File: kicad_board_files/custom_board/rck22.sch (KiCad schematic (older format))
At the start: 75 parts, among them IC1 PEC11L-4115F-S0020, J1 Conn_02x05_Odd_Even, J10 Conn_01x02, J2 USB_OTG, J3 PCC-SMP-K, J4 5V_DC_IN, J5 header, J6 SSR, J7 SSR, J8 SSR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

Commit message: Tweak the PCB silkscreen, add main UI graphic
Add some silkscreen text with version number and Logos
Add a graphic to be loaded from SD card for the main UI before reflow graph
Tweak the PCB layout and export new images from the 3D viewer
Update the README
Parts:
- added R18: 680/±1%/0.1W/0402, Resistor_SMD:R_0402_1005Metric, symbol Device:R_Small
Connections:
- net +3V3: now also R18.1
- net SWD_IO: now also R18.2
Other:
- note removed: "Commit message: "Add protection to thermocouple input\n\nUpdate the thermocouple interface with ferrite beads and filter capacitor\nAdd an alternative thermocouple connector other than terminal block\nAdd extra SSR lines for the case of multiple heaters\nReplace the 700mA 3.3V regulator with a 1A regulator, and replace its capacitors\nAdd 10K series resistors to the rotary encoder ouputs\nReplace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"
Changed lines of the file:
@@
-$EndComp
-$Comp
-L Connector_Generic:Conn_02x05_Odd_Even J1
-U 1 1 5D372FAD
-P 4650 3900
-F 0 "J1" H 4700 4317 50  0000 C CNN
-F 1 "Conn_02x05_Odd_Even" H 4700 4226 50  0000 C CNN
-F 2 "Connector_PinHeader_1.27mm:PinHeader_2x05_P1.27mm_Vertical_SMD" H 4650 3900 50  0001 C CNN
-F 3 "https://datasheet.lcsc.com/szlcsc/1907251430_Amphenol-ICC-20021221-00010C4LF_C180221.pdf" H 4650 3900 50  0001 C CNN
-F 4 "20021221-00010C4LF" H 4650 3900 50  0001 C CNN "Mfr. #"
-F 5 "C180221" H 4650 3900 50  0001 C CNN "LCSC #"
-F 6 "140" H 4650 3900 50  0001 C CNN "Stock"
-	1    4650 3900
-	1    0    0    -1
 $EndComp
 $Comp
@@
 $EndComp
 $Comp
-L sdcard_1051620101:sdcard_1051620101 conn1
-U 1 1 5D393514
-P 5050 1050
-F 0 "conn1" H 5050 1450 60  0000 C CNN
-F 1 "sdcard_1051620101" H 5200 500 60  0000 C CNN
-F 2 "connectors:sdcard_1051620101" H 5050 1050 60  0001 C CNN
-F 3 "https://www.molex.com/pdm_docs/sd/1051620101_sd.pdf" H 5050 1050 60  0001 C CNN
-F 4 "1051620101 " H 5050 1050 50  0001 C CNN "Mfr. #"
-F 5 "WM12823CT-ND" H 5050 1050 50  0001 C CNN "DK #"
-	1    5050 1050
-	1    0    0    -1
-$EndComp
-$Comp
 L Connector:TestPoint_Alt TP1
 U 1 1 5D394552
@@
 Wire Wire Line
 	8550 1200 8600 1200
-Text GLabel 4600 900  0    50   Input ~ 0
-SD_CS
-Text GLabel 4600 1000 0    50   Input ~ 0
-SD_MOSI
-Text GLabel 4600 1100 0    50   Input ~ 0
-SD_CLK
-Text GLabel 4600 1200 0    50   Input ~ 0
-SD_MISO
-NoConn ~ 4600 800
-NoConn ~ 4600 1300
-$Comp
-L power:+3V3 #PWR0103
-U 1 1 5D3982BB
-P 6200 1150
-F 0 "#PWR0103" H 6200 1000 50  0001 C CNN
-F 1 "+3V3" H 6200 1300 50  0000 C CNN
-F 2 "" H 6200 1150 50  0001 C CNN
-F 3 "" H 6200 1150 50  0001 C CNN
-	1    6200 1150
-	1    0    0    -1
-$EndComp
-$Comp
-L Device:C_Small C7
-U 1 1 5D398822
-P 6200 1400
-F 0 "C7" H 6090 1465 50  0000 L CNN
-F 1 "22uF/6.3V/±20%/0603" H 5730 1340 25  0000 L CNN
-F 2 "Capacitor_SMD:C_0603_1608Metric" H 6200 1400 50  0001 C CNN
-F 3 "https://datasheet.lcsc.com/szlcsc/Murata-Electronics-GRM188R71E104KA01D_C77050.pdf" H 6200 1400 50  0001 C CNN
-F 4 "GRM188R71E104KA01D" H 6200 1400 50  0001 C CNN "Mfr. #"
-F 5 "C77050" H 6200 1400 50  0001 C CNN "LCSC #"
-F 6 "334500" H 6200 1400 50  0001 C CNN "Stock"
-	1    6200 1400
-	1    0    0    -1
-$EndComp
-$Comp
-L power:GND #PWR0104
-U 1 1 5D398E24
-P 6200 1550
-F 0 "#PWR0104" H 6200 1300 50  0001 C CNN
-F 1 "GND" H 6205 1377 50  0000 C CNN
-F 2 "" H 6200 1550 50  0001 C CNN
-F 3 "" H 6200 1550 50  0001 C CNN
-	1    6200 1550
-	1    0    0    -1
-$EndComp
-$Comp
-L power:GND #PWR0105
-U 1 1 5D39A30B
-P 6100 850
-F 0 "#PWR0105" H 6100 600 50  0001 C CNN
-F 1 "GND" H 6105 677 50  0000 C CNN
-F 2 "" H 6100 850 50  0001 C CNN
-F 3 "" H 6100 850 50  0001 C CNN
-	1    6100 850
-	0    -1   -1   0
-$EndComp
-Wire Wire Line
-	5750 850  5950 850
-Wire Wire Line
-	5750 950  5950 950
-Wire Wire Line
-	6200 1150 6200 1200
-Wire Wire Line
-	5750 1200 6200 1200
-Connection ~ 6200 1200
-Text GLabel 5750 1100 2    50   Input ~ 0
-SD_SW
 $Comp
 L Device:C_Small C5
@@
 	0    -1   -1   0
 $EndComp
-Text GLabel 4950 3700 2    50   Input ~ 0
-SWD_IO
 Text GLabel 4950 3800 2    50   Input ~ 0
 SWD_CLK
@@
 $EndComp
 Wire Wire Line
-	4200 3700 4450 3700
+	4200 3700 4350 3700
 Text GLabel 4950 4000 2    50   Input ~ 0
 UART_RX
@@
 Connection ~ 1200 1550
 Wire Wire Line
-	5950 850  5950 950
-Wire Wire Line
-	6100 850  5950 850
-Connection ~ 5950 850
-Wire Wire Line
 	3600 7350 3600 7450
-Wire Wire Line
-	6200 1200 6200 1300
-Wire Wire Line
-	6200 1500 6200 1550
 Text GLabel 8200 4750 0    50   Input ~ 0
 SW
@@
 	1000 5950 1200 5950
 Connection ~ 1000 5950
-Text Notes 4100 1650 0    63   ~ 13
-SD Card
 Wire Notes Line
 	2991 6308 6805 6306
@@
 	4700 5550 4900 5550
 Connection ~ 4700 5550
-Text Notes 12450 2500 0    100  ~ 0
-Commit message: "Add protection to thermocouple input\n\nUpdate the thermocouple interface with ferrite beads and filter capacitor\nAdd an alternative thermocouple connector other than terminal block\nAdd extra SSR lines for the case of multiple heaters\nReplace the 700mA 3.3V regulator with a 1A regulator, and replace its capacitors\nAdd 10K series resistors to the rotary encoder ouputs\nReplace buttons with two pin header connectors so as to use momentary switches on the casing\nReverse UART connection in ARM SWD debug connector\nTune LED resistors to the datasheet parameters\nRearrange the schamtic and layout\nSource all components and generate a HTML BOM\nUpdate the README" \n
 $Comp
 L Power_Protection:NUP2105L D2
@@
 	8550 1050 8800 1050
 $Comp
-L myRF:karibe_logo L1
-U 1 1 5DD9A175
-P 1850 7150
-F 0 "L1" H 1737 7375 50  0000 C CNN
-F 1 "karibe_logo" H 1737 7284 50  0000 C CNN
-F 2 "artwork:karibe_logo" H 1850 7150 50  0001 C CNN
-F 3 "" H 1850 7150 50  0001 C CNN
-F 4 "1" H 1850 7150 50  0001 C CNN "DNP"
-	1    1850 7150
-	1    0    0    -1
-$EndComp
-$Comp
 L Graphic:Logo_Open_Hardware_Small #LOGO1
 U 1 1 5DDA873C
@@
 F 3 "~" H 10700 6850 50  0001 C CNN
 	1    10700 6850
-	1    0    0    -1
-$EndComp
-$Comp
-L power:GND #PWR0144
-U 1 1 5DDAE8C7
-P 1950 7150
-F 0 "#PWR0144" H 1950 6900 50  0001 C CNN
-F 1 "GND" H 1955 6977 50  0000 C CNN
-F 2 "" H 1950 7150 50  0001 C CNN
-F 3 "" H 1950 7150 50  0001 C CNN
-	1    1950 7150
 	1    0    0    -1
 $EndComp
@@
 Text Label 7850 3800 0    50   ~ 0
 DN
+Text GLabel 5050 3700 2    50   Input ~ 0
+SWD_IO
+$Comp
+L Connector_Generic:Conn_02x05_Odd_Even J1
+U 1 1 5D372FAD
+P 4650 3900
+F 0 "J1" H 4700 4200 50  0000 C CNN
+F 1 "Conn_02x05_Odd_Even" H 4850 3600 50  0000 C CNN
+F 2 "Connector_PinHeader_1.27mm:PinHeader_2x05_P1.27mm_Vertical_SMD" H 4650 3900 50  0001 C CNN
+F 3 "https://datasheet.lcsc.com/szlcsc/1907251430_Amphenol-ICC-20021221-00010C4LF_C180221.pdf" H 4650 3900 50  0001 C CNN
+F 4 "20021221-00010C4LF" H 4650 3900 50  0001 C CNN "Mfr. #"
+F 5 "C180221" H 4650 3900 50  0001 C CNN "LCSC #"
+F 6 "140" H 4650 3900 50  0001 C CNN "Stock"
+	1    4650 3900
+	1    0    0    -1
+$EndComp
+$Comp
+L Device:R_Small R18
+U 1 1 5DC1628C
+P 4700 3500
+F 0 "R18" V 4800 3450 50  0000 L CNN
+F 1 "680/±1%/0.1W/0402" V 4750 3300 25  0000 L CNN
+F 2 "Resistor_SMD:R_0402_1005Metric" H 4700 3500 50  0001 C CNN
+F 3 "https://datasheet.lcsc.com/szlcsc/1810191533_KOA-Speer-Elec-RK73H1ETTP6800F_C159998.pdf" H 4700 3500 50  0001 C CNN
+F 4 "RK73H1ETTP6800F" H 4700 3500 50  0001 C CNN "Mfr. #"
+F 5 "C159998" H 4700 3500 50  0001 C CNN "LCSC #"
+	1    4700 3500
+	0    -1   -1   0
+$EndComp
+Wire Wire Line
+	4950 3700 5000 3700
+Wire Wire Line
+	5000 3700 5000 3500
+Wire Wire Line
+	5000 3500 4800 3500
+Connection ~ 5000 3700
+Wire Wire Line
+	5000 3700 5050 3700
+Wire Wire Line
+	4600 3500 4350 3500
+Wire Wire Line
+	4350 3500 4350 3700
+Connection ~ 4350 3700
+Wire Wire Line
+	4350 3700 4450 3700
+$Comp
+L myRF:karibe_logo L1
+U 1 1 5DC493DB
+P 7350 6800
+F 0 "L1" H 7300 6700 50  0001 C CNN
+F 1 "karibe_logo" H 7350 6900 50  0001 C CNN
+F 2 "artwork:karibe_logo" H 7350 6800 50  0001 C CNN
+F 3 "" H 7350 6800 50  0001 C CNN
+F 4 "1" H 7350 6800 50  0001 C CNN "DNP"
+	1    7350 6800
+	1    0    0    -1
+$EndComp
+Text Notes 3905 1695 0    63   ~ 13
+SD Card
+Wire Wire Line
+	6200 1500 6200 1550
+Wire Wire Line
+	6200 1200 6200 1300
+Connection ~ 5950 850
+Wire Wire Line
+	6100 850  5950 850
+Wire Wire Line
+	5950 850  5950 950
+Text GLabel 5750 1100 2    50   Input ~ 0
+SD_SW
+Connection ~ 6200 1200
+Wire Wire Line
+	5750 1200 6200 1200
+Wire Wire Line
+	6200 1150 6200 1200
+Wire Wire Line
+	5750 950  5950 950
+Wire Wire Line
+	5750 850  5950 850
+$Comp
+L power:GND #PWR0105
+U 1 1 5D39A30B
+P 6100 850
+F 0 "#PWR0105" H 6100 600 50  0001 C CNN
+F 1 "GND" H 6105 677 50  0000 C CNN
+F 2 "" H 6100 850 50  0001 C CNN
+F 3 "" H 6100 850 50  0001 C CNN
+	1    6100 850
+	0    -1   -1   0
+$EndComp
+$Comp
+L power:GND #PWR0104
+U 1 1 5D398E24
+P 6200 1550
+F 0 "#PWR0104" H 6200 1300 50  0001 C CNN
+F 1 "GND" H 6205 1377 50  0000 C CNN
+F 2 "" H 6200 1550 50  0001 C CNN
+F 3 "" H 6200 1550 50  0001 C CNN
+	1    6200 1550
+	1    0    0    -1
+$EndComp
+$Comp
+L Device:C_Small C7
+U 1 1 5D398822
+P 6200 1400
+F 0 "C7" H 6090 1465 50  0000 L CNN
+F 1 "22uF/6.3V/±20%/0603" H 5730 1340 25  0000 L CNN
+F 2 "Capacitor_SMD:C_0603_1608Metric" H 6200 1400 50  0001 C CNN
+F 3 "https://datasheet.lcsc.com/szlcsc/Murata-Electronics-GRM188R71E104KA01D_C77050.pdf" H 6200 1400 50  0001 C CNN
+F 4 "GRM188R71E104KA01D" H 6200 1400 50  0001 C CNN "Mfr. #"
+F 5 "C77050" H 6200 1400 50  0001 C CNN "LCSC #"
+F 6 "334500" H 6200 1400 50  0001 C CNN "Stock"
+	1    6200 1400
+	1    0    0    -1
+$EndComp
+$Comp
+L power:+3V3 #PWR0103
+U 1 1 5D3982BB
+P 6200 1150
+F 0 "#PWR0103" H 6200 1000 50  0001 C CNN
+F 1 "+3V3" H 6200 1300 50  0000 C CNN
+F 2 "" H 6200 1150 50  0001 C CNN
+F 3 "" H 6200 1150 50  0001 C CNN
+	1    6200 1150
+	1    0    0    -1
+$EndComp
+NoConn ~ 4600 1300
+NoConn ~ 4600 800
+Text GLabel 4600 1200 0    50   Input ~ 0
+SD_MISO
+Text GLabel 4600 1100 0    50   Input ~ 0
+SD_CLK
+Text GLabel 4600 1000 0    50   Input ~ 0
+SD_MOSI
+Text GLabel 4600 900  0    50   Input ~ 0
+SD_CS
+$Comp
+L sdcard_1051620101:sdcard_1051620101 conn1
+U 1 1 5D393514
+P 5050 1050
+F 0 "conn1" H 5050 1450 60  0000 C CNN
+F 1 "sdcard_1051620101" H 5200 500 60  0000 C CNN
+F 2 "connectors:sdcard_1051620101" H 5050 1050 60  0001 C CNN
+F 3 "https://www.molex.com/pdm_docs/sd/1051620101_sd.pdf" H 5050 1050 60  0001 C CNN
+F 4 "1051620101 " H 5050 1050 50  0001 C CNN "Mfr. #"
+F 5 "WM12823CT-ND" H 5050 1050 50  0001 C CNN "DK #"
+	1    5050 1050
+	1    0    0    -1
+$EndComp
 $EndSCHEMATC

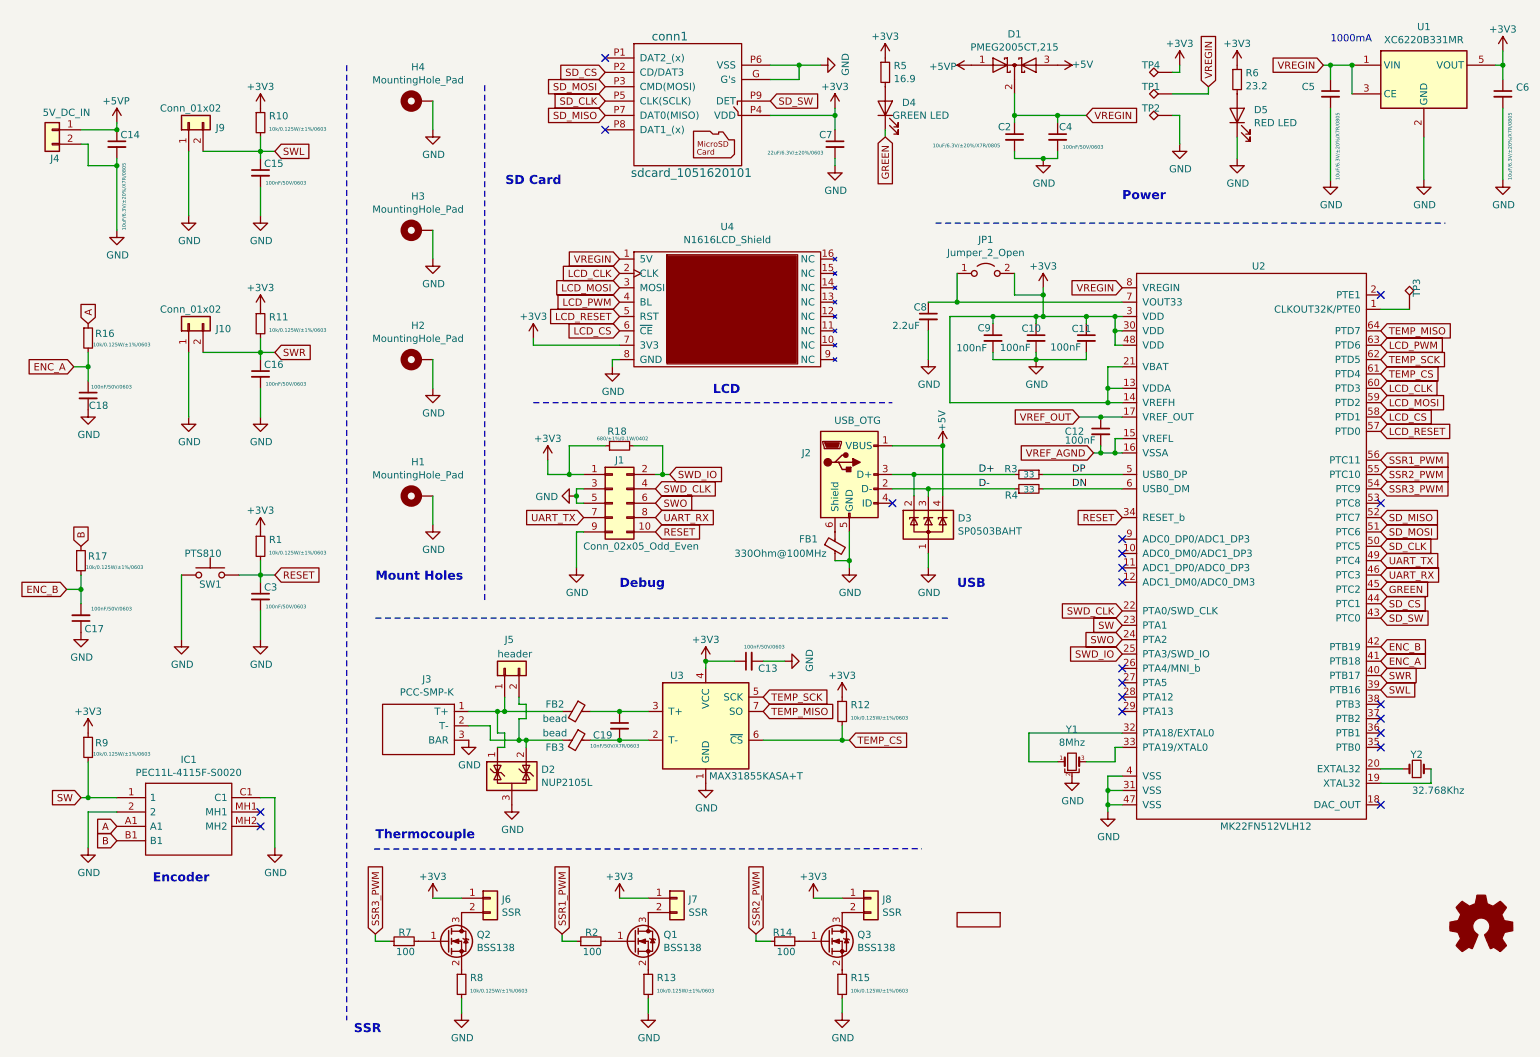
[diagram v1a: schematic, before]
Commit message: touch up the board
Re-assign some GPIOs to simplify routing
Mark SMD components as surface mount in their properties
Re-arrange power connector and status LEDs
Replace the SD card component with one readily available at LCSC.com
Add optional on-board SMD PTS810 buttons
Change some capacitor footprints from 0402 to 0805 to reduce BOM items
Add more details on the silkscreen: dimensions, jlcpcb customer identifier placeholder e.t.c
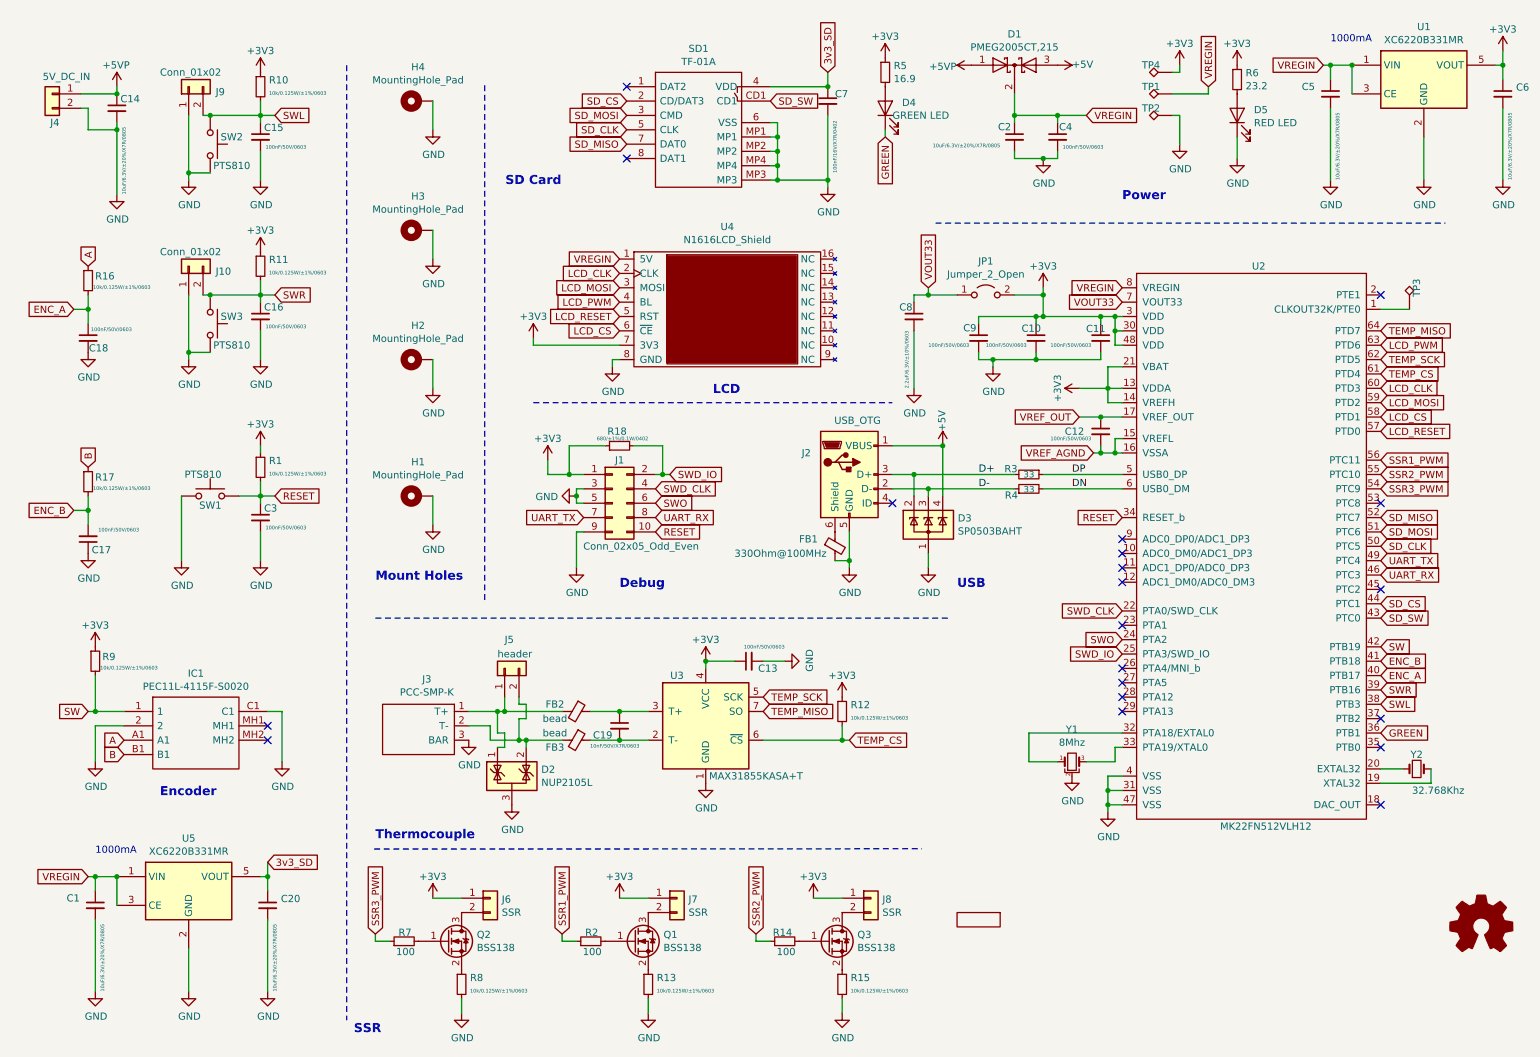
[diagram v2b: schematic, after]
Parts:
- removed conn1: sdcard_1051620101, connectors:sdcard_1051620101, symbol sdcard_1051620101:sdcard_1051620101
- added C1, C20: 10uF/6.3V/±20%/X7R/0805, Capacitor_SMD:C_0805_2012Metric, symbol Device:C_Small
- added SD1: TF-01A, connectors:TF01A, symbol TF01A:TF-01A
- added SW2, SW3: PTS810, Button_Switch_SMD:SW_SPST_PTS810, symbol Switch:SW_Push
- added U5: XC6220B331MR, Package_TO_SOT_SMD:SOT-23-5, symbol Regulator_Linear:XC6220B331MR
- C10, C11, C12, C9: value 100nF -> 100nF/50V/0603
- C5, C6: footprint Capacitor_SMD:C_0402_1005Metric -> Capacitor_SMD:C_0805_2012Metric
- C7: value 22uF/6.3V/±20%/0603 -> 100nF/16V/X7R/0402; footprint Capacitor_SMD:C_0603_1608Metric -> Capacitor_SMD:C_0402_1005Metric; LCSC # C77050 -> C85857; Mfr. # GRM188R71E104KA01D -> GCM155R71C104KA55D; Stock 334500 -> (none); Value (none) -> 100nF/16V/X7R/0402
- C8: value 2.2uF -> 2.2uF/6.3V/±10%/0603
- IC1: Manufacturer_Name Bourns -> (none)
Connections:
- net +3V3: no longer C7.1
- net ENC_A: now also U2.40 (PTB17); no longer U2.41 (PTB18)
- net ENC_B: now also U2.41 (PTB18); no longer U2.42 (PTB19)
- net GND: now also C1.2, C20.2, SD1.6 (VSS), SD1.MP1, SD1.MP2, SD1.MP3, SD1.MP4, SW2.2, SW3.2, U5.2 (GND)
- net GREEN: now also U2.36 (PTB1); no longer U2.45 (PTC2)
- net SD_CLK: now also SD1.5 (CLK)
- net SD_CS: now also SD1.2 (CD/DAT3)
- net SD_MISO: now also SD1.7 (DAT0)
- net SD_MOSI: now also SD1.3 (CMD)
- net SD_SW: now also SD1.CD1
- net SW: now also U2.42 (PTB19); no longer U2.23 (PTA1)
- net SWL: now also U2.38 (PTB3), SW2.1; no longer U2.39 (PTB16)
- net SWR: now also U2.39 (PTB16), SW3.1; no longer U2.40 (PTB17)
- net VREGIN: now also C1.1, U5.1 (VIN), U5.3 (CE)
- net VOUT33: now reaches C8.1, JP1.1 (A), U2.7 (VOUT33)
- new net 3v3_SD: C20.1, C7.1, SD1.4 (VDD), U5.5 (VOUT)
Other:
- moved on the sheet: C11, C14, C15, C16, C17, C18, C3, C7, C8, C9, IC1, J10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
